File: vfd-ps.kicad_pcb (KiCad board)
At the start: 2 copper layers, 58 x 45 mm, 51 parts, among them J1 Conn_01x04, J2 Conn_01x04, J3 Conn_01x04, U1 TPS54360DDA, U2 LM4871

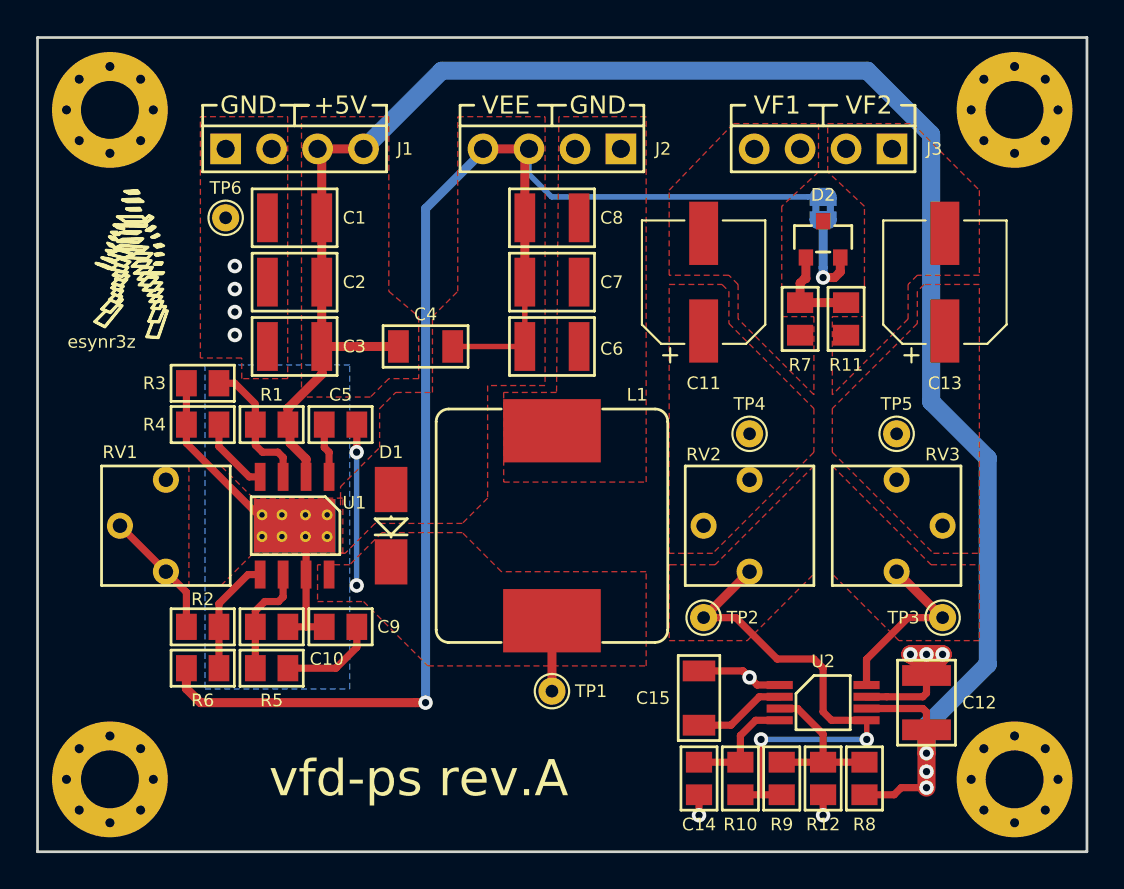
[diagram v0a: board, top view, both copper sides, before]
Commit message: Remove all local libs and switch to submodule library
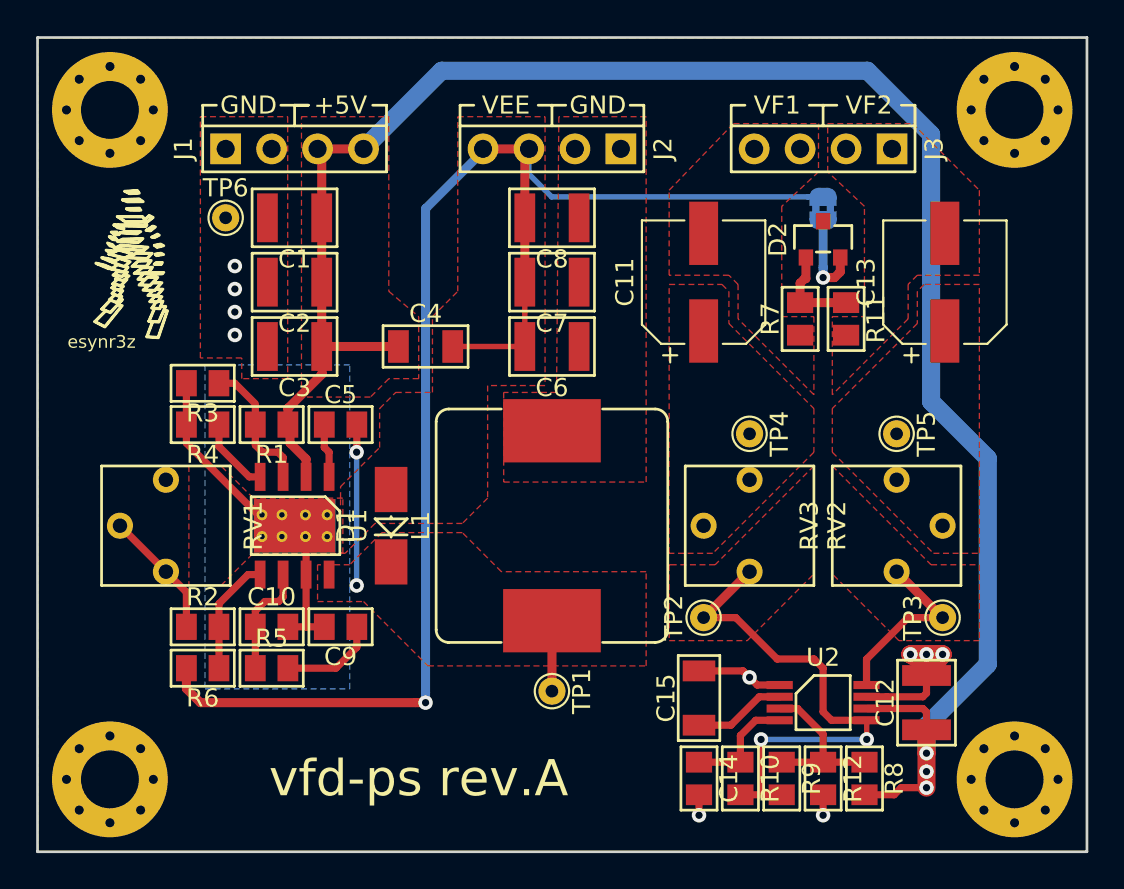
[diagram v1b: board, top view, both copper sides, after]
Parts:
- C1, C12, C2, C3, C6, C7, C8: footprint lib_fp:C_1210 -> esynr3z_Capacitor:C_1210
- C10, C14, C5, C9: footprint lib_fp:C_0805 -> esynr3z_Capacitor:C_0805
- C11, C13: footprint lib_fp:CP_Elec_6.3x7.7 -> esynr3z_Capacitor:CP_Elec_6.3x7.7
- C15, C4: footprint lib_fp:C_1206 -> esynr3z_Capacitor:C_1206
- D1: footprint lib_fp:SMA -> esynr3z_Diode:SMA
- D2: footprint lib_fp:SOT-23 -> esynr3z_SOT:SOT-23
- G***: footprint fp_lib:iv18_draw -> esynr3z_Symbol:iv18_draw
- G***: footprint fp_lib:esynr3z_logo_4.5x8.4mm_Silk -> esynr3z_Symbol:esynr3z_logo_4.5x8.4mm_Silk
- J1, J2, J3: footprint lib_fp:PinHeader_1x04_P2.54mm_Vertical -> esynr3z_Connector:PinHeader_1x04_P2.54mm_Vertical
- JP1: footprint lib_fp:SolderJumper-2_P1.3mm_Bridged2Bar_RoundedPad1.0x1.5mm -> esynr3z_Jumper:SolderJumper-2_P1.3mm_Bridged2Bar_RoundedPad1.0x1.5mm
- L1: footprint lib_fp:Sumida_CDRH127 -> esynr3z_Inductor:Sumida_CDRH127
- R1, R10, R11, R12, R2, R3, R4, R5, R6, R7, R8, R9: footprint lib_fp:R_0805 -> esynr3z_Resistor:R_0805
- REF** (x4): footprint fp_lib:MountingHole_3.2mm_M3_Pad_Via -> esynr3z_Mechanical:MountingHole_3.2mm_M3_Pad_Via
- RV1, RV2, RV3: footprint lib_fp:Bourns_3362P -> esynr3z_Potentiometer:Bourns_3362P
- TP1, TP2, TP3, TP4, TP5, TP6: footprint lib_fp:TestPoint_THTPad_D1.5mm_Drill0.7mm -> esynr3z_TestPoint:TestPoint_THTPad_D1.5mm_Drill0.7mm
- U1: footprint lib_fp:TI_SO-PowerPAD-8_ThermalVias -> esynr3z_SO:TI_SO-PowerPAD-8_ThermalVias
- U2: footprint lib_fp:VSSOP-8_3.0x3.0mm_P0.65mm -> esynr3z_SO:VSSOP-8_3.0x3.0mm_P0.65mm

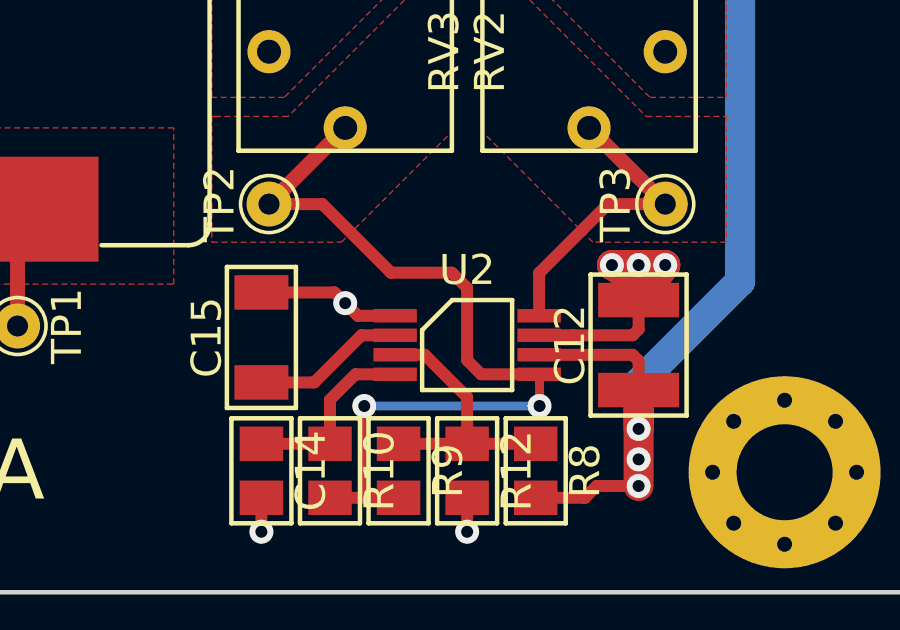
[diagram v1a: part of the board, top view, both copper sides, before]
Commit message: Replace lm4871 footprint
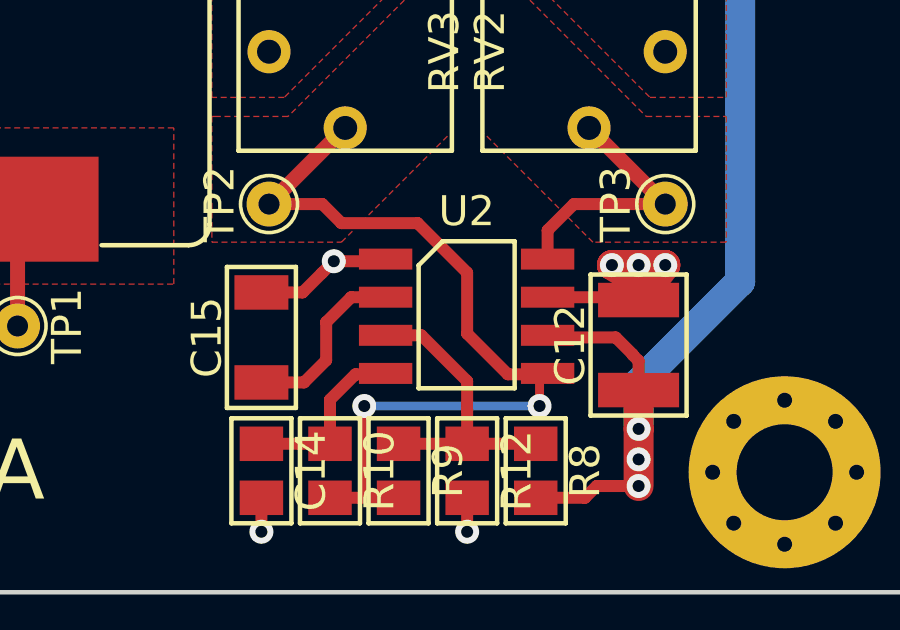
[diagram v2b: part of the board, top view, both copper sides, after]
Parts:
- R2: value 16k -> 36k
- R6: value 1k -> 2.2k
- RV1: value 20k -> 50k
- U2: footprint esynr3z_SO:VSSOP-8_3.0x3.0mm_P0.65mm -> esynr3z_SO:SOIC-8_3.9x4.9mm_P1.27mm
- moved U2 0.96 mm to (161.4, 110.8)
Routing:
- net GND: track 18.5 -> 17.1 mm
- net Net-(RV3-Pad1): track 10.2 -> 8.84 mm
- net Net-(C15-Pad1): track 5.11 -> 6.06 mm
- net Net-(R12-Pad1): track 9.11 -> 10.0 mm

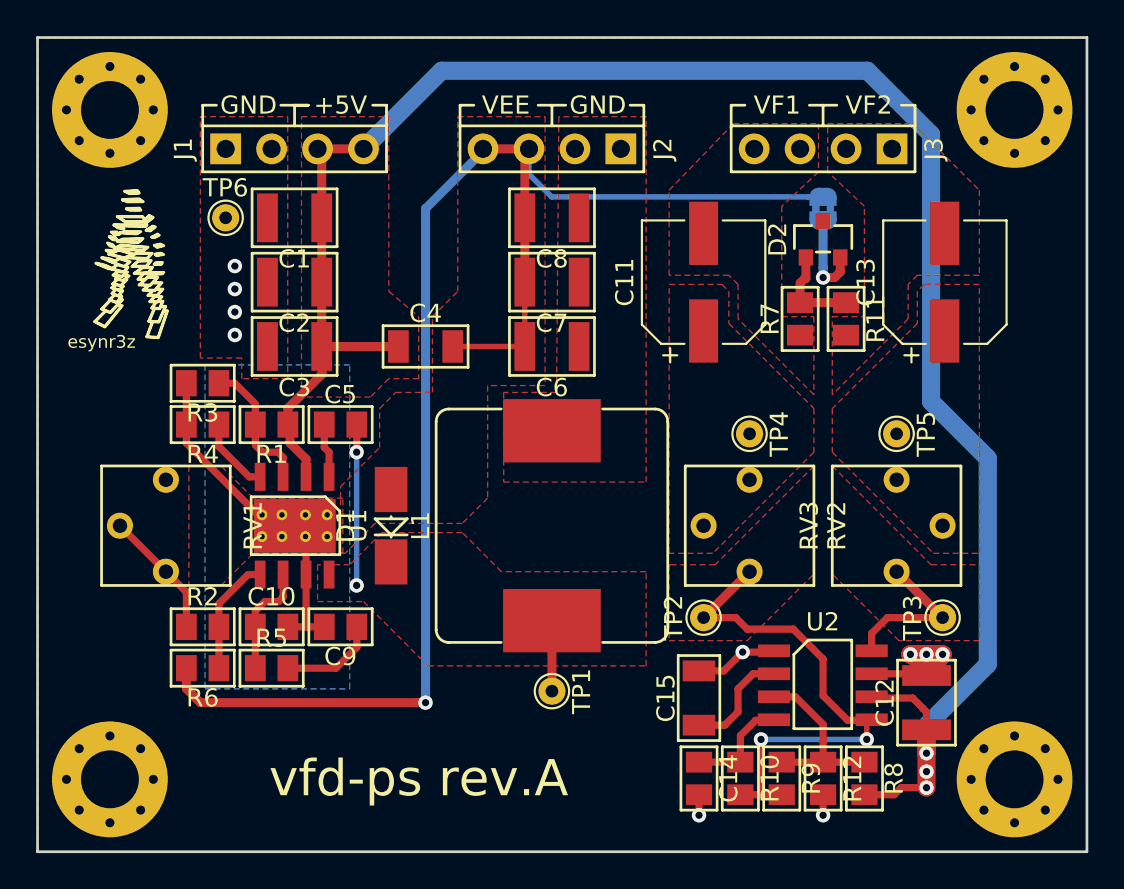
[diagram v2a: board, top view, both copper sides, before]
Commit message: Align labels on silk and fab layers
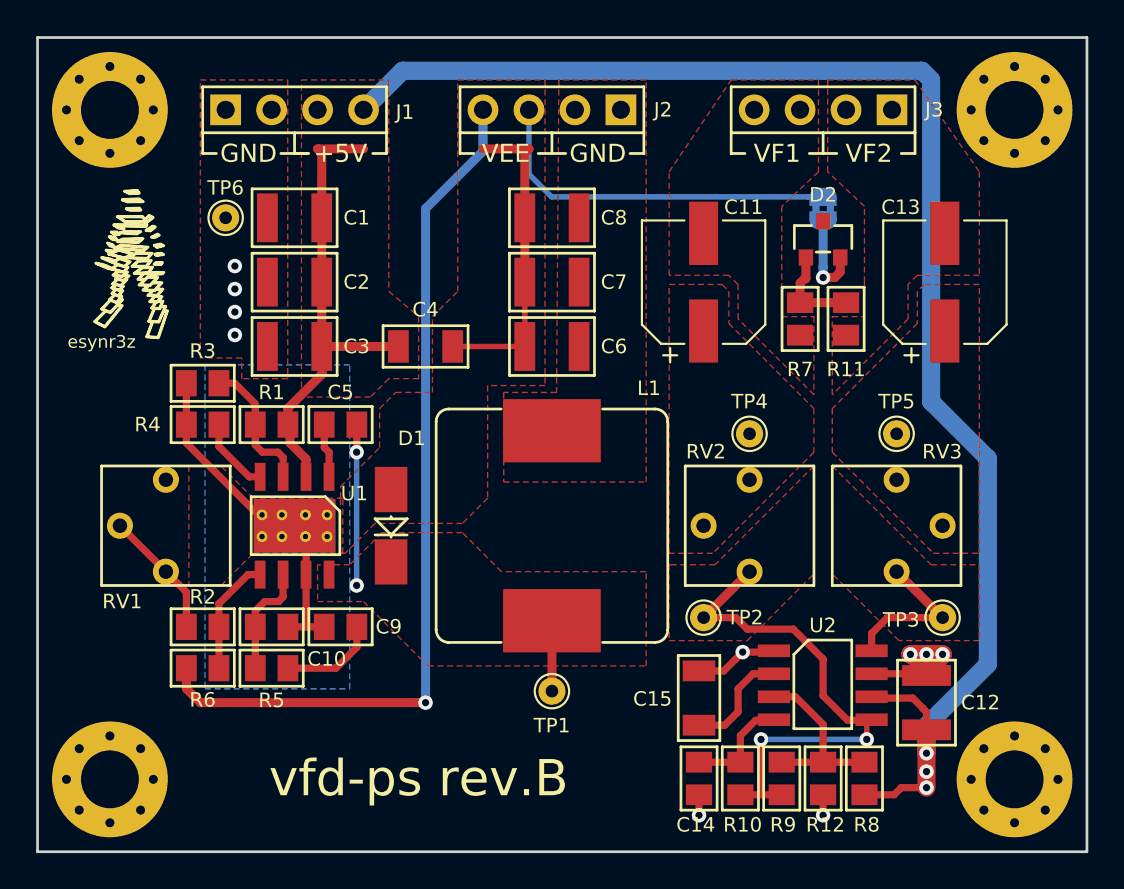
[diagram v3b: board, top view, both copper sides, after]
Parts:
- moved J1 2.16 mm to (128.4, 79.0)
- moved J2 2.16 mm to (150.2, 79.0)
- moved J3 2.16 mm to (165.2, 79.0)
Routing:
- net GNDPAD: track 98.3 -> 102.8 mm
- net +5V: track 108.9 -> 109.8 mm
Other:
- board text added: "vfd-ps rev.B"
- board text removed: "vfd-ps rev.A"
